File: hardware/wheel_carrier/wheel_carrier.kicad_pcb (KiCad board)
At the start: 2 copper layers, 96 x 122 mm, 44 parts, among them J1 开发板左排 20P, J10 遥控·前差速, J11 遥控·后差速, J12 BEC 输入 6~7.4V, J13 扩展·左排(直连 J1), J14 扩展·右排(直连 J2), J15 电源排针, J2 开发板右排 20P, J3 霍尔·左前, J4 霍尔·右前, J5 霍尔·左后, J6 霍尔·右后, J7 舵机·前差速, J8 舵机·后差速, J9 遥控·模式, U1 LM2596T-5

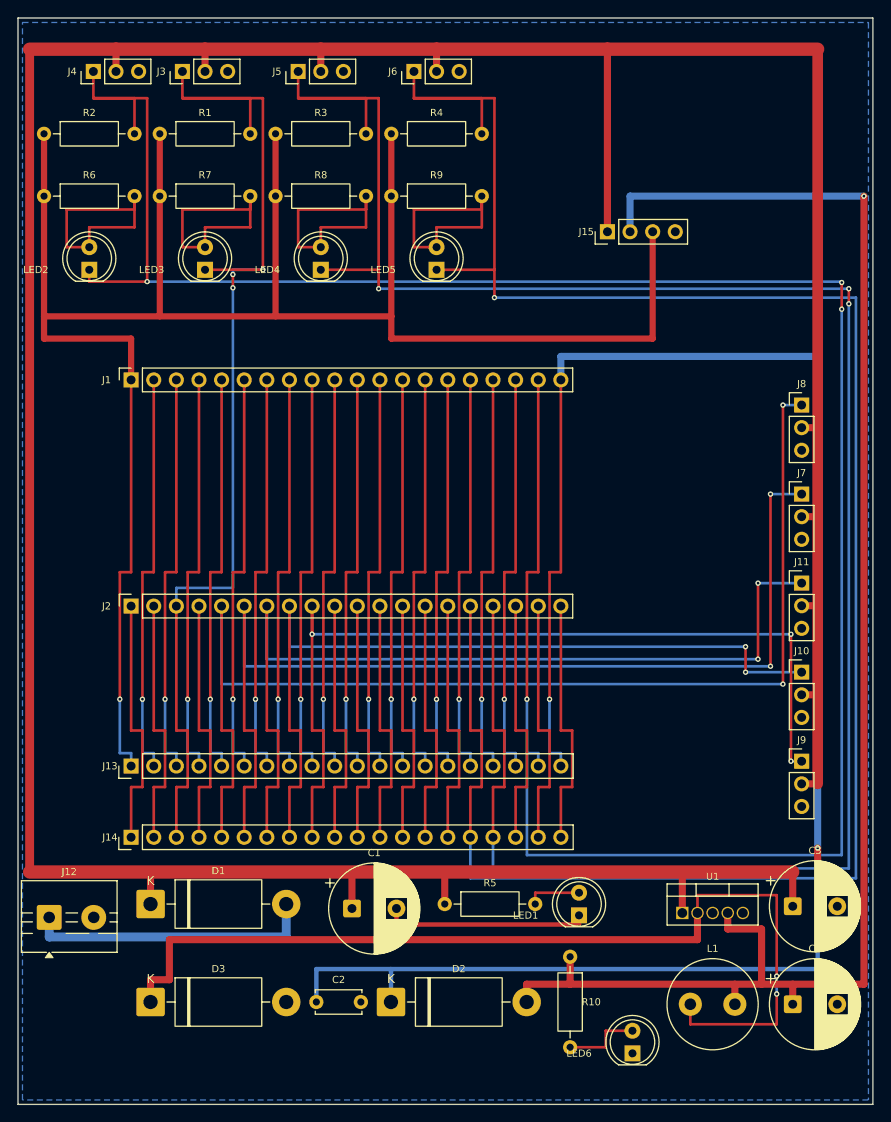
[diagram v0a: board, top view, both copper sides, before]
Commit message: feat(hw): PCB 补全丝印：接口功能/GPIO、每针网名、电源脚极性
板子此前只有位号与封装自带丝印，接线插板全靠翻 README，补齐：
- 九个接口功能名+GPIO 号，3 针接口标注 S/+V/G；J15 四脚竖排词标、
  J12 端子下方 +/- 极性与输入电压；电源母线 +BEC/+3V3/+5V、指示灯用途
- J1/J2/J13/J14 每一针网名错行排印，1 脚实心三角标，右端 J13=J1/J14=J2
- 网名由网表生成（原理图改了 GPIO 分配会直接构建报错，不印过期号）；
  新增 check_silk() 几何自检：逐条文字对焊盘开窗/板边/彼此做包围盒检查
- 顺带挪正 6 个压焊盘或邻件丝印的位号（LED1/LED6/C1/C4/R10/J15），
  丝印类 DRC 告警从 30 条清零；kicad_pro 版号写 3，避免 KiCad 迁移
  改写时丢掉 lib_footprint_mismatch 的忽略配置
- 预览图与 gerber 包按新丝印重导

Co-Authored-By: Claude Code <noreply@anthropic.com>
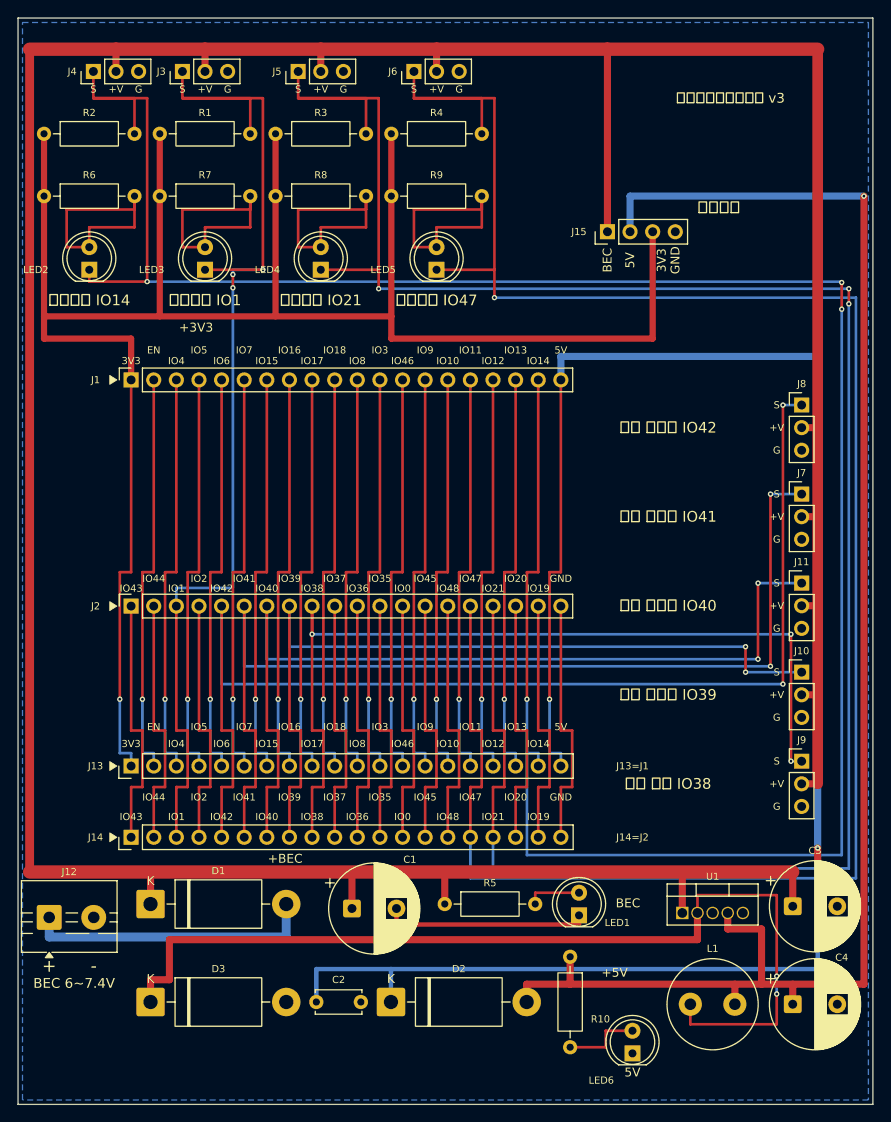
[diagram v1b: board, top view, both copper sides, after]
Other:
- board text added: "+"
- board text added: "+3V3"
- board text added: "+5V"
- board text added: "+BEC"
- board text added: "+V"
- board text added: "-"
- board text added: "3V3"
- board text added: "5V"
- board text added: "BEC"
- board text added: "BEC 6~7.4V"
- board text added: "EN"
- board text added: "G"
- board text added: "GND"
- board text added: "IO0"
- board text added: "IO1"
- board text added: "IO10"
- board text added: "IO11"
- board text added: "IO12"
- board text added: "IO13"
- board text added: "IO14"
- board text added: "IO15"
- board text added: "IO16"
- board text added: "IO17"
- board text added: "IO18"
- board text added: "IO19"
- board text added: "IO2"
- board text added: "IO20"
- board text added: "IO21"
- board text added: "IO3"
- board text added: "IO35"
- board text added: "IO36"
- board text added: "IO37"
- board text added: "IO38"
- board text added: "IO39"
- board text added: "IO4"
- board text added: "IO40"
- board text added: "IO41"
- board text added: "IO42"
- board text added: "IO43"
- board text added: "IO44"
- board text added: "IO45"
- board text added: "IO46"
- board text added: "IO47"
- board text added: "IO48"
- board text added: "IO5"
- board text added: "IO6"
- board text added: "IO7"
- board text added: "IO8"
- board text added: "IO9"
- board text added: "J13=J1"
- board text added: "J14=J2"
- board text added: "S"
- board text added: "右前霍尔 IO14"
- board text added: "右后霍尔 IO47"
- board text added: "左前霍尔 IO1"
- board text added: "左后霍尔 IO21"
- board text added: "电源排针"
- board text added: "舵机 前差速 IO41"
- board text added: "舵机 后差速 IO42"
- board text added: "轮速监测台转接底板 v3"
- board text added: "遥控 前差速 IO39"
- board text added: "遥控 后差速 IO40"
- board text added: "遥控 模式 IO38"

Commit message: feat(hw): v4 改版：2×8 电源条、电调/油门直通口，铺铜缝合与丝印电压标注
- J15 从 1×4 扩成 2×8 电源条（BEC×2 / 5V×3 / 3V3×3，其余 8 针全 GND，
  每列「电源+地」相邻）——一根 2.54 针只插得下一根杜邦线，传感器多了
  原版 4 针不够分；丝印把每个电源脚的电压竖标在所在列正上方，下排两端标 GND
- 新增 J16「电调 BEC 输入」与 J17「接收机·油门」：电调 3 针插头直接进板
  （三针中间必为 +V，插反不反电源），油门信号经板载纯铜直通走线到 J17
  再回接收机——板子不通电也照传；J12 螺丝端子保留，进电只允许一个来源
- 铺铜：J1 上方那条带子（v3 起就被霍尔信号线/焊盘排净空围成孤岛、被
  自动删除）用一根 0.3mm GND 线从第 8/9 针间隙缝回主铺铜，重填后铺满
- gen_pcb 增加 .kicad_pro 自愈：kicad-cli 重写工程文件会丢掉
  lib_footprint_mismatch 的降级忽略（21 条警告复活），每次生成自动补回
- 验证：ERC 0；丝印几何自检 181 条通过；DRC 除已知孤岛提示外零违规；
  预览图与 gerber 包全部重导

Co-Authored-By: Claude Code <noreply@anthropic.com>
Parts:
- added J16: 电调·BEC输入, Connector_PinHeader_2.54mm:PinHeader_1x03_P2.54mm_Vertical, F.Cu at (6.50, 53.5)
- added J17: 接收机·油门, Connector_PinHeader_2.54mm:PinHeader_1x03_P2.54mm_Vertical, F.Cu at (6.50, 69.5)
- J15: footprint Connector_PinHeader_2.54mm:PinHeader_1x04_P2.54mm_Vertical -> Connector_PinHeader_2.54mm:PinHeader_2x08_P2.54mm_Vertical
- moved J15 14.6 mm to (80.8, 24.0), turned to -90 degrees
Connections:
- J15 pad 2: +5V -> GND
- J15 pad 3: +3V3 -> +BEC
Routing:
- net THROTTLE: track 0.00 -> 20.0 mm
- net +BEC: track 408.3 -> 421.3 mm
- net +3V3: track 227.7 -> 218.3 mm
- net GND: track 51.8 -> 59.8 mm
- net +5V: track 178.0 -> 178.7 mm, vias 1 -> 2
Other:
- board text added: "接收机 油门"
- board text added: "电调 BEC 输入"
- board text added: "轮速监测台转接底板 v4"
- board text removed: "电源排针"
- board text removed: "轮速监测台转接底板 v3"

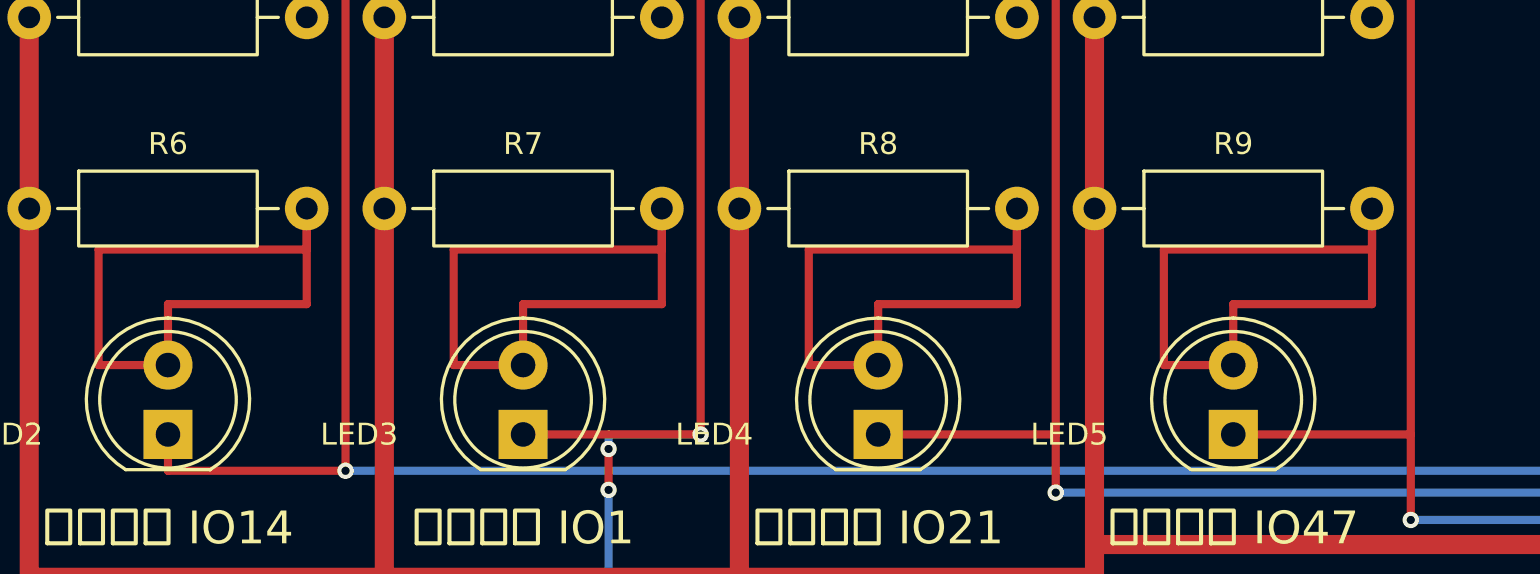
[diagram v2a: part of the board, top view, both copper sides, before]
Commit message: fix(hw): 铺铜 min_thickness 修复地网断点；去掉 LED 链 A 网的重复走线
- 未连接项目的根因修复：铺铜最小填充厚度沿用 KiCad 默认 0.254，密集区
  （电源条下方等窄缝）填不进去，整张 GND 网被悄悄撕成互不相通的两片
  （DRC 报「未连接项目」，断点还牵扯开发板地脚 J2.20/J14.20）。调到 0.2
  （≥ 设计规则下限）后整片连通，DRC 全零——丝印、连接、封装比对全部干净
- 删掉 LED2~LED5 的 A 网重复走线：330R→LED 的同一段连接在最初版布线里
  写了两条路径（同网双线不属任何 DRC 错误类，一路静默留存），删去冗余
  的一条，每网回到单一路径
- README：验证状态改「DRC 全零」、已知接受项按 min_thickness 根因重写、
  铺铜一节补教训；预览图与打样包按新板重导

Co-Authored-By: Claude Code <noreply@anthropic.com>
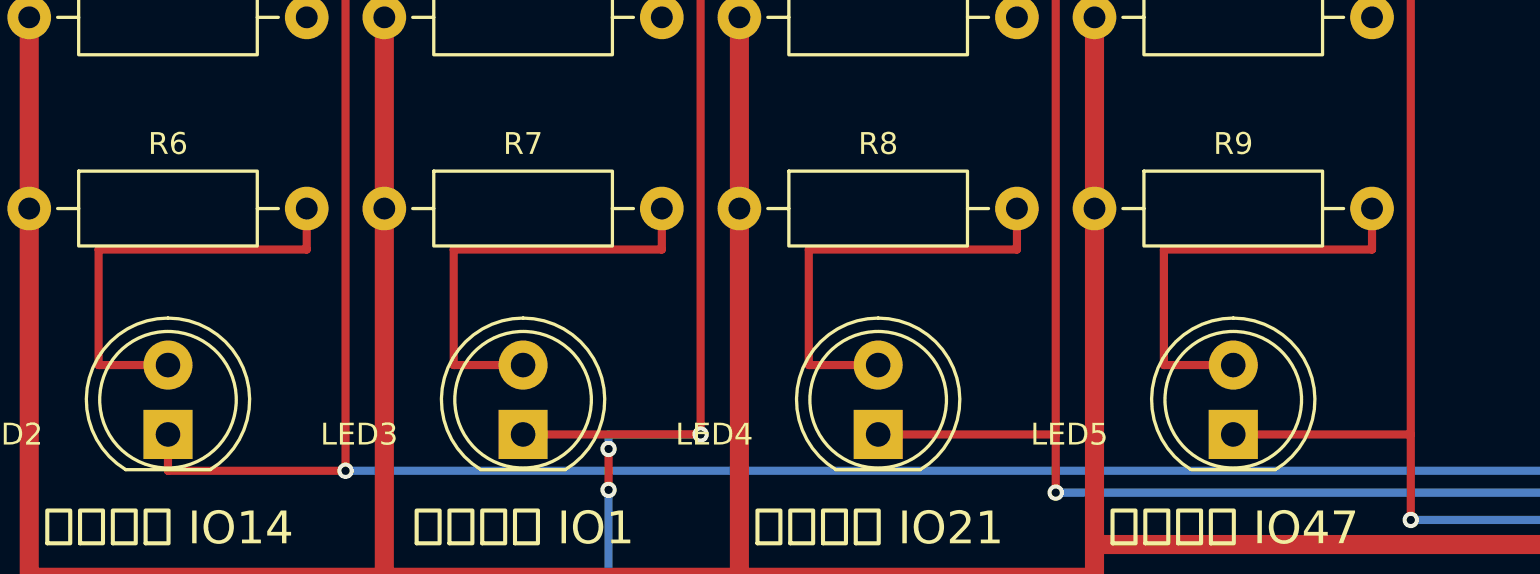
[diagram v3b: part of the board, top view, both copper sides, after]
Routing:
- net Net-(LED2-A): track 26.7 -> 15.9 mm
- net Net-(LED5-A): track 26.7 -> 15.9 mm
- net Net-(LED4-A): track 26.7 -> 15.9 mm
- net Net-(LED3-A): track 26.7 -> 15.9 mm
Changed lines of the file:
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@@
-	)
-	(segment
-		(start 8 23.5)
-		(end 8 25.73)
-		(width 0.3)
-		(layer "F.Cu")
-		(net "Net-(LED2-A)")
 	)
 	(segment
 		(start 13.08 20)
 		(end 13.08 21.5)
-		(width 0.3)
-		(layer "F.Cu")
-		(net "Net-(LED2-A)")
-	)
-	(segment
-		(start 13.08 23.5)
-		(end 8 23.5)
 		(width 0.3)
 		(layer "F.Cu")
@@
 	)
 	(segment
-		(start 13.08 20)
-		(end 13.08 23.5)
-		(width 0.3)
-		(layer "F.Cu")
-		(net "Net-(LED2-A)")
-	)
-	(segment
 		(start 26.08 21.5)
 		(end 18.46 21.5)
@@
 		(start 18.46 25.73)
 		(end 21 25.73)
-		(width 0.3)
-		(layer "F.Cu")
-		(net "Net-(LED3-A)")
-	)
-	(segment
-		(start 26.08 23.5)
-		(end 21 23.5)
 		(width 0.3)
 		(layer "F.Cu")
@@
 		(layer "F.Cu")
 		(net "Net-(LED3-A)")
-	)
-	(segment
-		(start 26.08 20)
-		(end 26.08 23.5)
-		(width 0.3)
-		(layer "F.Cu")
-		(net "Net-(LED3-A)")
-	)
-	(segment
-		(start 21 23.5)
-		(end 21 25.73)
-		(width 0.3)
-		(layer "F.Cu")
-		(net "Net-(LED3-A)")
-	)
-	(segment
-		(start 39.08 23.5)
-		(end 34 23.5)
-		(width 0.3)
-		(layer "F.Cu")
-		(net "Net-(LED4-A)")
-	)
-	(segment
-		(start 39.08 20)
-		(end 39.08 23.5)
-		(width 0.3)
-		(layer "F.Cu")
-		(net "Net-(LED4-A)")
 	)
 	(segment
@@
 	)
 	(segment
-		(start 34 23.5)
-		(end 34 25.73)
-		(width 0.3)
-		(layer "F.Cu")
-		(net "Net-(LED4-A)")
-	)
-	(segment
 		(start 52.08 20)
 		(end 52.08 21.5)
-		(width 0.3)
-		(layer "F.Cu")
-		(net "Net-(LED5-A)")
-	)
-	(segment
-		(start 52.08 23.5)
-		(end 47 23.5)
-		(width 0.3)
-		(layer "F.Cu")
-		(net "Net-(LED5-A)")
-	)
-	(segment
-		(start 52.08 20)
-		(end 52.08 23.5)
 		(width 0.3)
 		(layer "F.Cu")
@@
 		(start 44.46 21.5)
 		(end 44.46 25.73)
-		(width 0.3)
-		(layer "F.Cu")
-		(net "Net-(LED5-A)")
-	)
-	(segment
-		(start 47 23.5)
-		(end 47 25.73)
 		(width 0.3)
 		(layer "F.Cu")
@@
 			(clearance 0.508)
 		)
-		(min_thickness 0.254)
+		(min_thickness 0.2)
 		(fill yes
 			(thermal_gap 0.508)
